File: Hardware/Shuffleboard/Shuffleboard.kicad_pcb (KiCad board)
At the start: 4 copper layers, 130 x 131.5 mm, 69 parts, among them IC1 DG3157EDL-T1-GE3, IC2 DG3157EDL-T1-GE3, J1 1869279, J2 1869279, J3 Conn_01x10, Q1 NMOS, U1 COM-09032, U2 PAM8302AAS, U3 LMV331, U4 INND-TS56RCB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

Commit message: layout
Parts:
- moved R20 31.2 mm to (152.5, 42.0), turned to 90 degrees
- moved R21 22.9 mm to (150.0, 42.0), turned to 90 degrees
- moved R16 22.8 mm to (160.0, 42.0), turned to 90 degrees
- moved R19 22.4 mm to (150.0, 51.0), turned to -90 degrees
- moved R15 21.5 mm to (157.5, 42.0), turned to 90 degrees
- moved R18 19.6 mm to (152.5, 51.0), turned to -90 degrees
- moved R17 16.2 mm to (157.5, 50.9), turned to -90 degrees
- moved R22 13.8 mm to (160.0, 51.0), turned to -90 degrees
- moved C10 3.61 mm to (170.5, 38.0)
- moved C11 1.69 mm to (172.5, 49.9), turned to 90 degrees
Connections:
- J2 pad 1: /Connector/PB8_MOSI(PICO) -> /PB8_MOSI
- J2 pad 2: /Connector/PB9_SPI_CLK -> /PB9_SPI_CLK
- J2 pad 3: /Connector/PB16_LATCH_PULSE -> /PB16_L/P
- U6 pad 11: /7Seg/PB9_SPI_CLK -> /PB9_SPI_CLK
- U6 pad 12: /7Seg/PB16_LATCH_PULSE -> /PB16_L/P
- U6 pad 14: /7Seg/PB8_MOSI(PICO) -> /PB8_MOSI
- U8 pad 11: /7Seg/PB9_SPI_CLK -> /PB9_SPI_CLK
- U8 pad 12: /7Seg/PB16_LATCH_PULSE -> /PB16_L/P
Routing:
- net /PB8_MOSI: track 0.00 -> 64.8 mm, vias 0 -> 2
- net /PB9_SPI_CLK: track 0.00 -> 54.9 mm, vias 0 -> 3
- net /PB16_L/P: track 0.00 -> 51.5 mm, vias 0 -> 1
- net Net-(U6-QE): track 0.00 -> 38.3 mm, vias 0 -> 2
- net Net-(U6-QD): track 0.00 -> 31.8 mm, vias 0 -> 2
- net Net-(U6-QG): track 0.00 -> 31.2 mm, vias 0 -> 2
- net Net-(U6-QF): track 0.00 -> 29.3 mm
- net Net-(U6-QC): track 0.00 -> 27.3 mm, vias 0 -> 2
- net Net-(U6-QB): track 0.00 -> 23.3 mm
- net Net-(U6-QH): track 0.00 -> 22.2 mm, vias 0 -> 2
- net Net-(U6-QA): track 0.00 -> 19.6 mm
- net /7Seg/PB16_LATCH_PULSE: track 12.2 -> 0.00 mm
- net Net-(U6-QH*): track 0.00 -> 8.92 mm
- net Net-(R17-Pad2): track 0.00 -> 2.29 mm
- net Net-(R21-Pad2): track 0.00 -> 2.26 mm
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
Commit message: layout 2
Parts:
- added TP1: GND, TestPoint:TestPoint_THTPad_1.5x1.5mm_Drill0.7mm, F.Cu at (213.4, 27.8)
- H1, H2, H3, H4, H5, H6: footprint MountingHole:MountingHole_2.2mm_M2 -> MountingHole:MountingHole_2.2mm_M2_DIN965_Pad
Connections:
- net Net-(U6-QH*) renamed /7Seg/QH1
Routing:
- net +3.3V: track 67.3 -> 65.3 mm, vias 15 -> 14
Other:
- board text added: "GND"
- board text added: "PWR"
- board text added: "Player 1"
- board text added: "Player 2"
- board text removed: "Power"

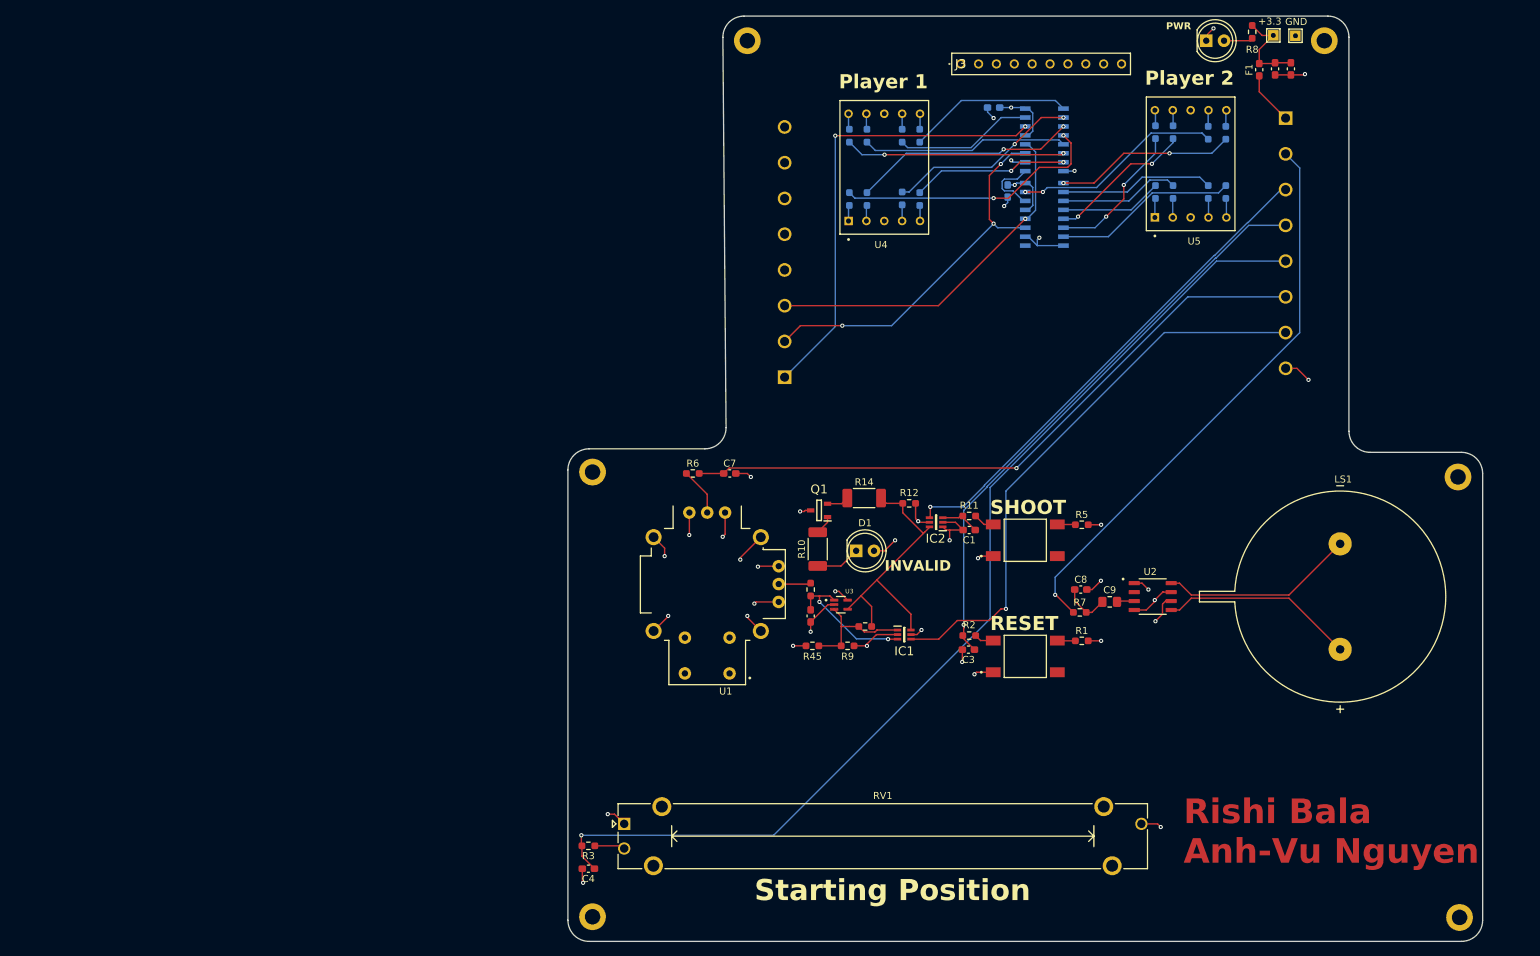
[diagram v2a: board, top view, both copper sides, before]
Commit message: footprint for lcd
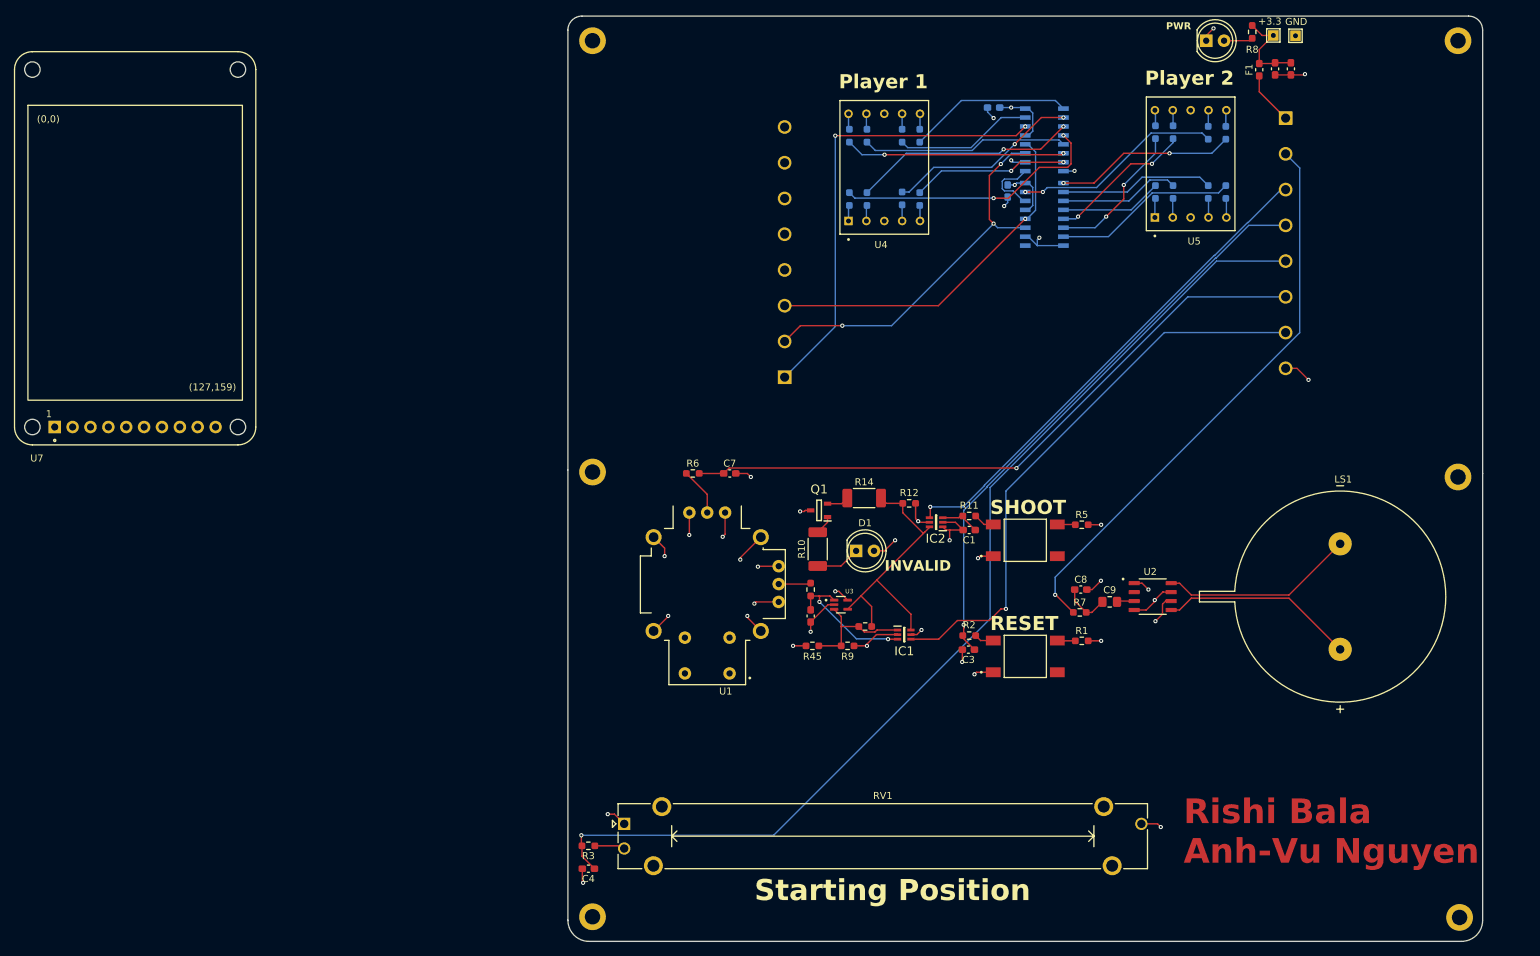
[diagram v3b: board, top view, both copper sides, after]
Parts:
- removed J3: Conn_01x10, ShuffleboardFootprints:CES-110-XX-Y-S
- added U7: Adafruit ST7735R, Footprint:adafruit_st7735r, F.Cu at (48.5, 58.0)
- moved H2 22.0 mm to (113.5, 28.5)
- moved H3 19.0 mm to (236.5, 28.5)
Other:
- outline, holes or cut-outs redrawn
